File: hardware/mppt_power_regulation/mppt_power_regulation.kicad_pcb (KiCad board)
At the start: 2 copper layers, 100 x 90 mm, 77 parts, among them IC101 LMR38010SDDAR, IC102 TPS2121, J101 CT3151, J102 CT3151, J103 CT3151, J104 CT3151, J105 CT3151, J106 CT3151, J107 CT3151, J108 CT3151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

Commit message: gave names to unlabeled nets
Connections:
- net Net-(D101-A) renamed /12to5LED
- net Net-(D102-A) renamed /5VISO_LED
- net Net-(D104-A) renamed /12MUXLED
- net Net-(D106-A) renamed /5to3V3LED
- net Net-(IC101-BOOT) renamed /BOOT_VINto12
- net Net-(IC101-EN) renamed /EN_VINto12
- net Net-(IC101-FB) renamed /FB_VINto12
- net Net-(IC101-RT/SYNC) renamed /RT/Sync
- net Net-(IC101-SW) renamed /SW_VINto12
- net Net-(IC101-VIN) renamed /+V_ARR
- net Net-(IC102-CP2) renamed /CP2
- net Net-(IC102-ILIM) renamed /ILIM
- net Net-(IC102-PR1) renamed /PR1
- net Net-(IC102-SS) renamed /SS
- net Net-(PS101-+VOUT) renamed /5VISO_RAW
- net Net-(R101-Pad2) renamed /FB_inner
- net Net-(R119-Pad2) renamed /EN_inner
- net Net-(U101-SW) renamed /SW_12to5

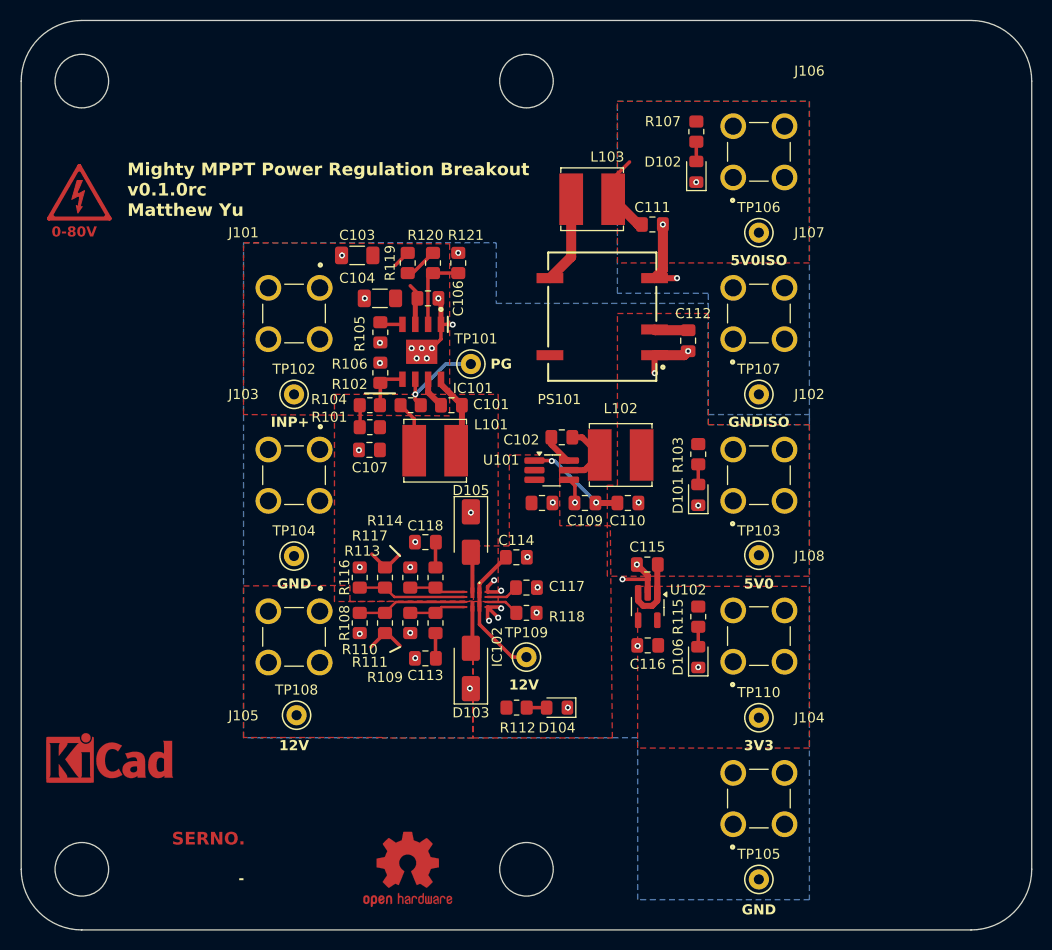
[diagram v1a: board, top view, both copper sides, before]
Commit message: moved testpoints from between connectors to free space on board, added labels under banana jacks
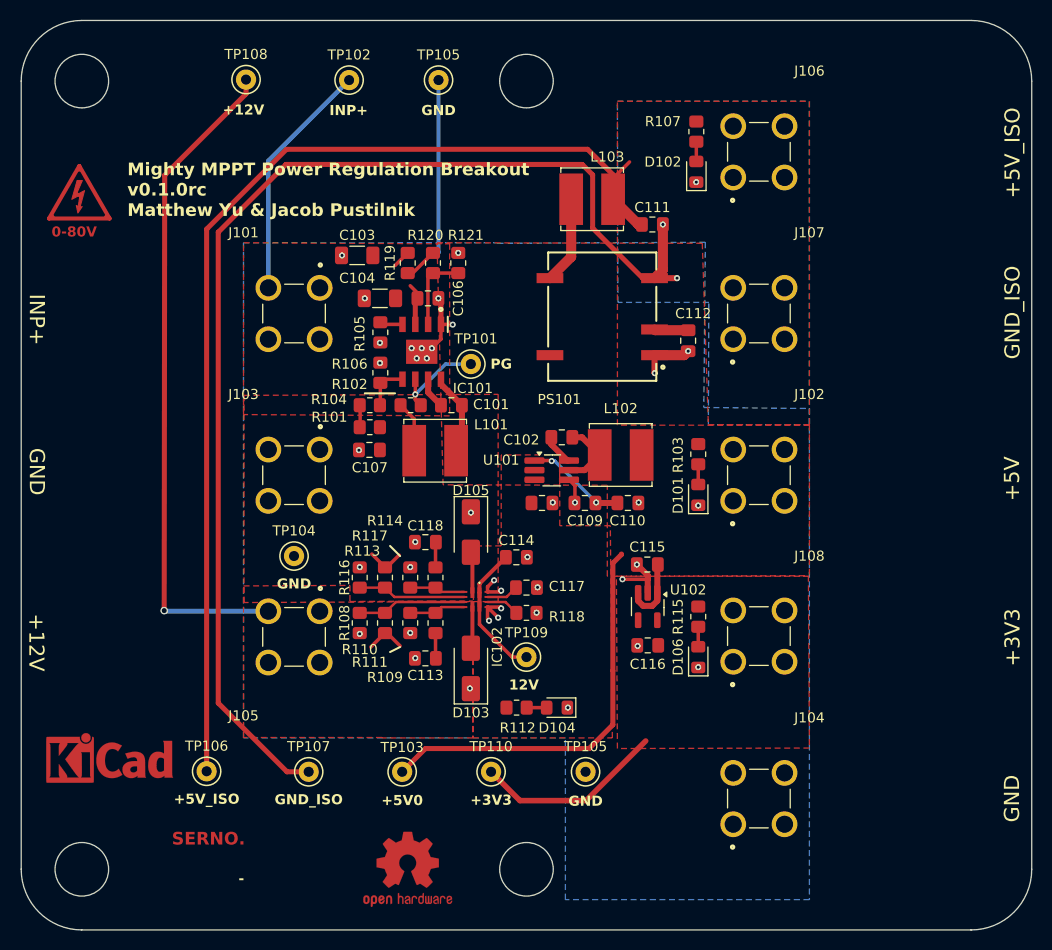
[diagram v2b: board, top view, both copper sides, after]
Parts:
- added TP105: TestPoint, TestPoint:TestPoint_Keystone_5000-5004_Miniature, F.Cu at (71.3, 35.9)
- moved TP106 76.3 mm to (48.4, 104.3)
- moved TP108 63.1 mm to (52.2, 35.9)
- moved TP107 58.1 mm to (58.5, 104.3)
- moved TP103 41.3 mm to (67.7, 104.3)
- moved TP102 31.6 mm to (62.5, 35.9)
- moved TP110 27.0 mm to (76.5, 104.3)
- moved TP105 20.2 mm to (85.8, 104.3)
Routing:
- net GND1: track 7.89 -> 120.0 mm
- net +5VP: track 8.25 -> 108.9 mm
- net +12L: track 10.7 -> 77.0 mm, vias 0 -> 1
- net +5V: track 20.2 -> 60.2 mm
- net /+V_ARR: track 5.43 -> 29.3 mm
- net +3V3: track 0.00 -> 18.9 mm
- net GND: track 28.0 -> 45.0 mm
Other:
- board text added: "+12V"
- board text added: "+3V3"
- board text added: "+5V"
- board text added: "+5V0"
- board text added: "+5V_ISO"
- board text added: "GND_ISO"
- board text added: "Mighty MPPT Power Regulation Breakout v0.1.0rc Matthew Yu & Jacob Pustilnik"
- board text removed: "3V3"
- board text removed: "5V0"
- board text removed: "5V0ISO"
- board text removed: "GNDISO"
- board text removed: "Mighty MPPT Power Regulation Breakout v0.1.0rc Matthew Yu"

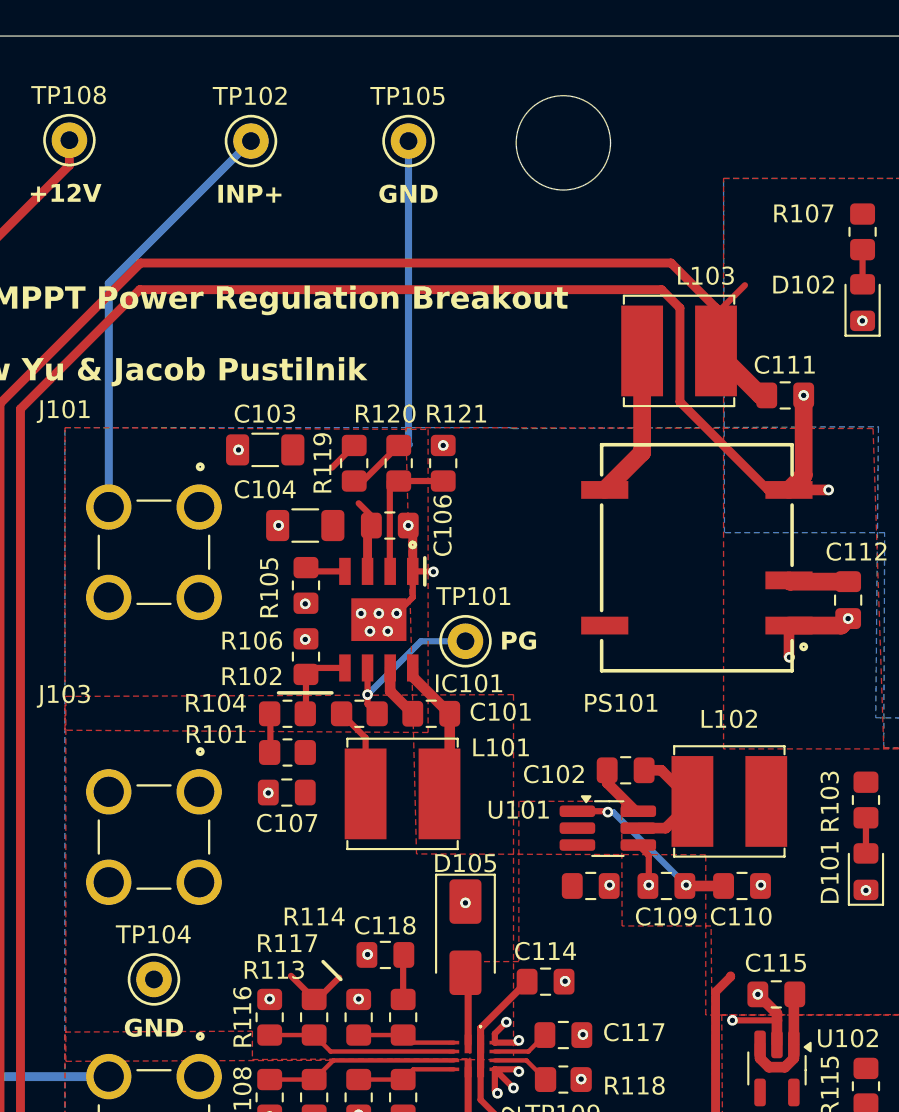
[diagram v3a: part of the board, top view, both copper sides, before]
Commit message: fix drc errors introduced into converter, power reg
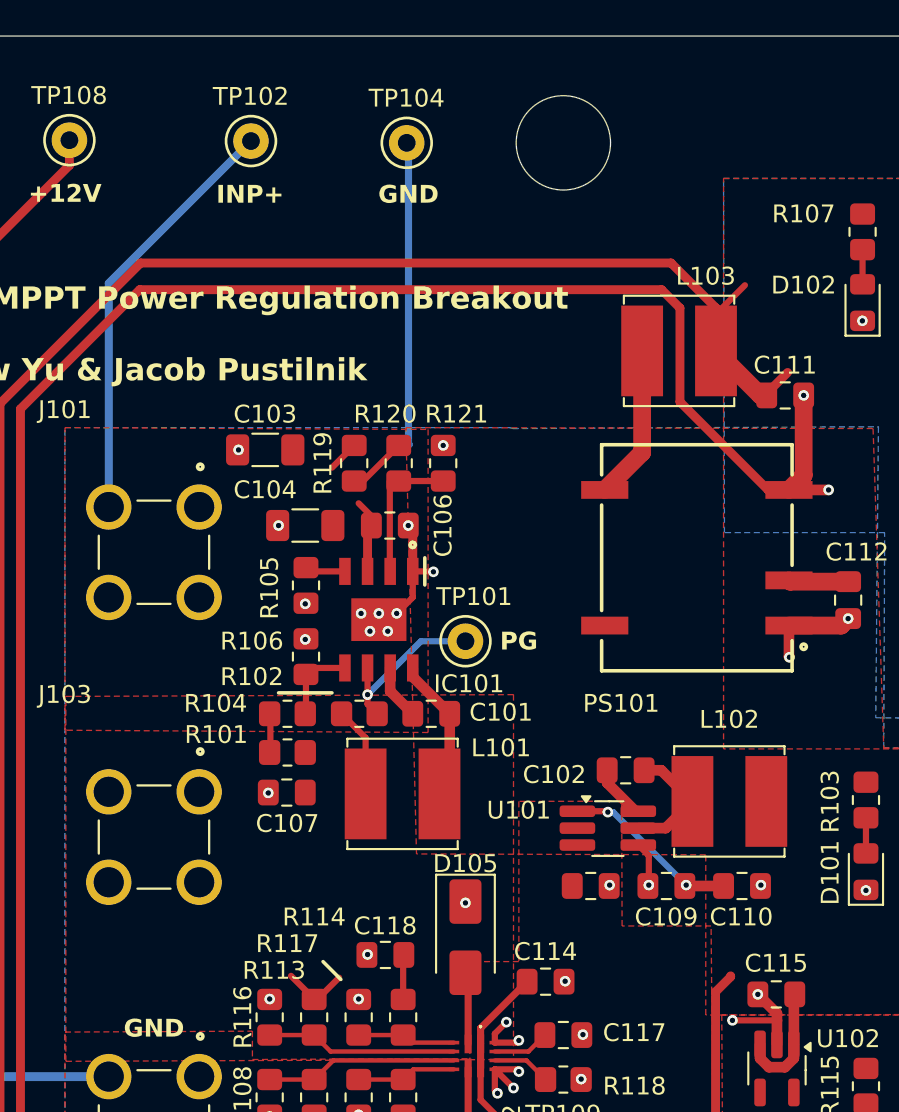
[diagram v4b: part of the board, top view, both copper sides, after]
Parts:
- removed the TP105 at (71.3, 35.9)
- C111: value 4.7u -> 10u
- moved TP104 49.1 mm to (71.2, 36.0)
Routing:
- net +5VP: track 108.9 -> 110.6 mm
